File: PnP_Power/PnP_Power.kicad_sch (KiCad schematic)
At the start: 0 parts

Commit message: Progress
Schematic has everything but 12V jack and H-bridge Vac DC motor control
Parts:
- added A1: A000067, PnP_Footprints:ARDUINO_A000067, symbol PnP_symbols:A000067
- added C1, C2, C3, C4, C5, C6: 82uF, Capacitor_THT:CP_Radial_D8.0mm_P2.50mm, symbol Device:C_Polarized
- added D1, D2: GREEN, LED_SMD:LED_0603_1608Metric_Pad1.05x0.95mm_HandSolder, symbol Device:LED
- added J1: S2B-PH-K-SLFSN, PnP_Footprints:CONN_S2B-PH-K-S_JST, symbol PnP_symbols:S2B-PH-K-SLFSN
- added J2, J3, J4, J5, J6, J7: S4B-PH-K-SLFSN, PnP_Footprints:CONN_S4B-PH-K-S_JST, symbol PnP_symbols:S4B-PH-K-SLFSN
- added R1: 1.5k, Resistor_SMD:R_0603_1608Metric_Pad0.98x0.95mm_HandSolder, symbol Device:R_US
- added R2: 2.2k, Resistor_SMD:R_0603_1608Metric_Pad0.98x0.95mm_HandSolder, symbol Device:R_US
- added R3: 820, Resistor_SMD:R_0603_1608Metric_Pad0.98x0.95mm_HandSolder, symbol Device:R_US
- added U1, U2, U3, U4, U5, U6: ~, PnP_Footprints:A4988, symbol PnP_symbols:A4988
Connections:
- new net: J4.1, U3.6 (2B)
- new net: J4.2, U3.5 (2A)
- new net: J4.3, U3.4 (1A)
- new net: J4.4, U3.3 (1B)
- new net: D1.2 (A), R2.2
- new net: J5.1, U4.6 (2B)
- new net: J5.2, U4.5 (2A)
- new net: J5.3, U4.4 (1A)
- new net: J5.4, U4.3 (1B)
- new net: J7.1, U6.6 (2B)
- new net: J7.2, U6.5 (2A)
- new net: J7.3, U6.4 (1A)
- new net: J7.4, U6.3 (1B)
- new net: D2.2 (A), R3.2
- new net: J6.1, U5.6 (2B)
- new net: J6.2, U5.5 (2A)
- new net: J6.3, U5.4 (1A)
- new net: J6.4, U5.3 (1B)
- new net: J1.1, R1.2
- new net: J2.1, U1.6 (2B)
- new net: J2.2, U1.5 (2A)
- new net: J2.3, U1.4 (1A)
- new net: J2.4, U1.3 (1B)
- new net: J3.4, U2.3 (1B)
- new net: J3.3, U2.4 (1A)
- new net: J3.2, U2.5 (2A)
- new net: J3.1, U2.6 (2B)
- new net +12V: A1.VIN, C1.1, C2.1, C3.1, C4.1, C5.1, C6.1, R2.1, U1.8 (VMOT), U2.8 (VMOT), U3.8 (VMOT), U4.8 (VMOT), U5.8 (VMOT), U6.8 (VMOT)
- new net +5V: R3.1, U1.2 (VDD), U2.2 (VDD), U3.2 (VDD), U4.2 (VDD), U5.2 (VDD), U6.2 (VDD)
- new net DIR1: U1.9 (Direction)
- new net DIR2: U2.9 (Direction)
- new net DIR3: U3.9 (Direction)
- new net DIR4: U4.9 (Direction)
- new net DIR5: U5.9 (Direction)
- new net DIR6: U6.9 (Direction)
- new net EN1: U1.16 (ENABLE)
- new net EN2: U2.16 (ENABLE)
- new net EN3: U3.16 (ENABLE)
- new net EN4: U4.16 (ENABLE)
- new net EN5: U5.16 (ENABLE)
- new net EN6: U6.16 (ENABLE)
- new net GND: C1.2, C2.2, C3.2, C4.2, C5.2, C6.2, D1.1 (K), D2.1 (K), J1.2, U1.1 (GND), U1.7 (GND), U2.1 (GND), U2.7 (GND), U3.1 (GND), U3.7 (GND), U4.1 (GND), U4.7 (GND), U5.1 (GND), U5.7 (GND), U6.1 (GND), U6.7 (GND)
- new net MS1_1: U1.15 (MS1)
- new net MS1_2: U2.15 (MS1)
- new net MS1_3: U3.15 (MS1)
- new net MS1_4: U4.15 (MS1)
- new net MS1_5: U5.15 (MS1)
- new net MS1_6: U6.15 (MS1)
- new net MS2_1: U1.14 (MS2)
- new net MS2_2: U2.14 (MS2)
- new net MS2_3: U3.14 (MS2)
- new net MS2_4: U4.14 (MS2)
- new net MS2_5: U5.14 (MS2)
- new net MS2_6: U6.14 (MS2)
- new net MS3_1: U1.13 (MS3)
- new net MS3_2: U2.13 (MS3)
- new net MS3_3: U3.13 (MS3)
- new net MS3_4: U4.13 (MS3)
- new net MS3_5: U5.13 (MS3)
- new net MS3_6: U6.13 (MS3)
- new net RES1: U1.12 (Reset)
- new net RES2: U2.12 (Reset)
- new net RES3: U3.12 (Reset)
- new net RES4: U4.12 (Reset)
- new net RES5: U5.12 (Reset)
- new net RES6: U6.12 (Reset)
- new net SLP1: U1.11 (Sleep)
- new net SLP2: U2.11 (Sleep)
- new net SLP3: U3.11 (Sleep)
- new net SLP4: U4.11 (Sleep)
- new net SLP5: U5.11 (Sleep)
- new net SLP6: U6.11 (Sleep)
- new net STEP1: U1.10 (Step)
- new net STEP2: U2.10 (Step)
- new net STEP3: U3.10 (Step)
- new net STEP4: U4.10 (Step)
- new net STEP5: U5.10 (Step)
- new net STEP6: U6.10 (Step)
- new net WHITE_LED: R1.1
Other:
- note added: "NEMA 17 A Axis"
- note added: "NEMA 17 COMP FEED"
- note added: "NEMA 17 X Axis"
- note added: "NEMA 17 Y Axis 1"
- note added: "NEMA 17 Y Axis 2"
- note added: "NEMA 17 Z Axis"
- note added: "Power LEDs"
- note added: "White LED"

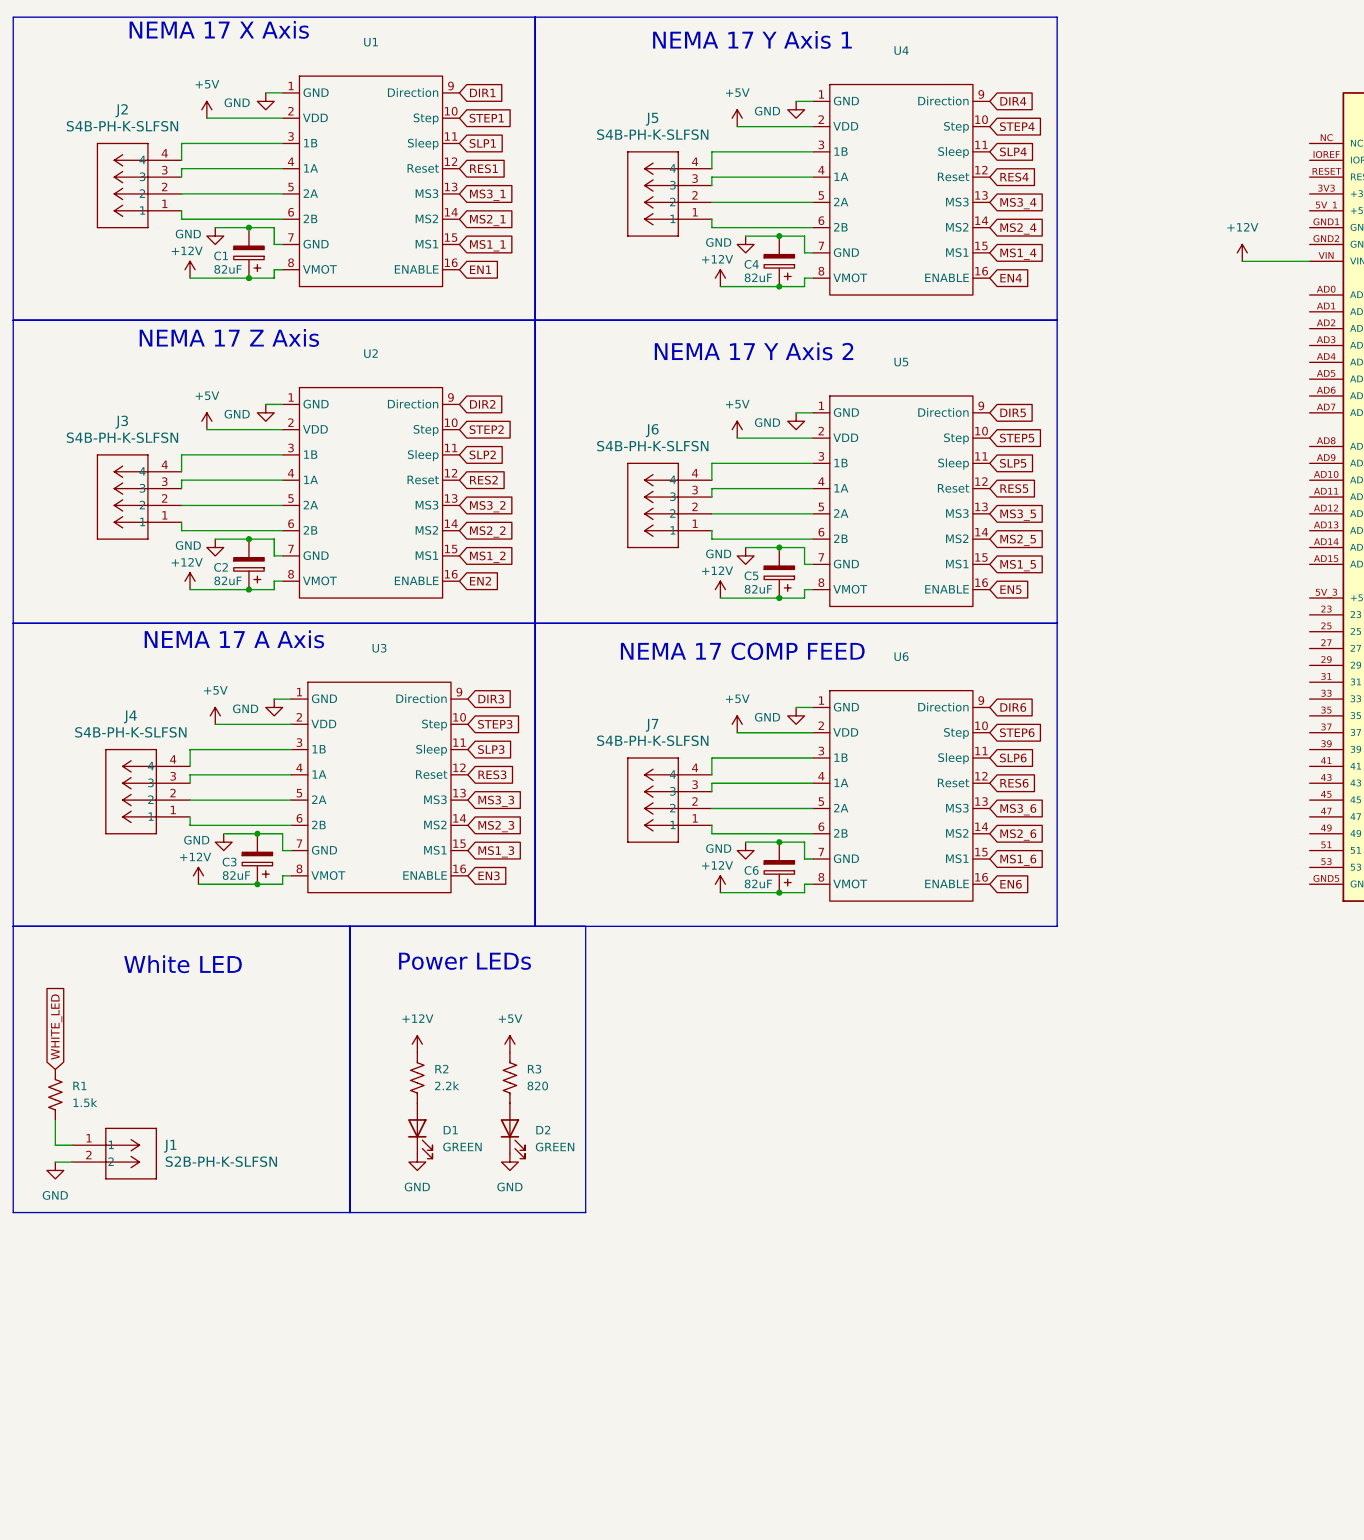
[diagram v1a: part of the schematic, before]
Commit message: Connectors changed, H-bridge VNH added, white leds done
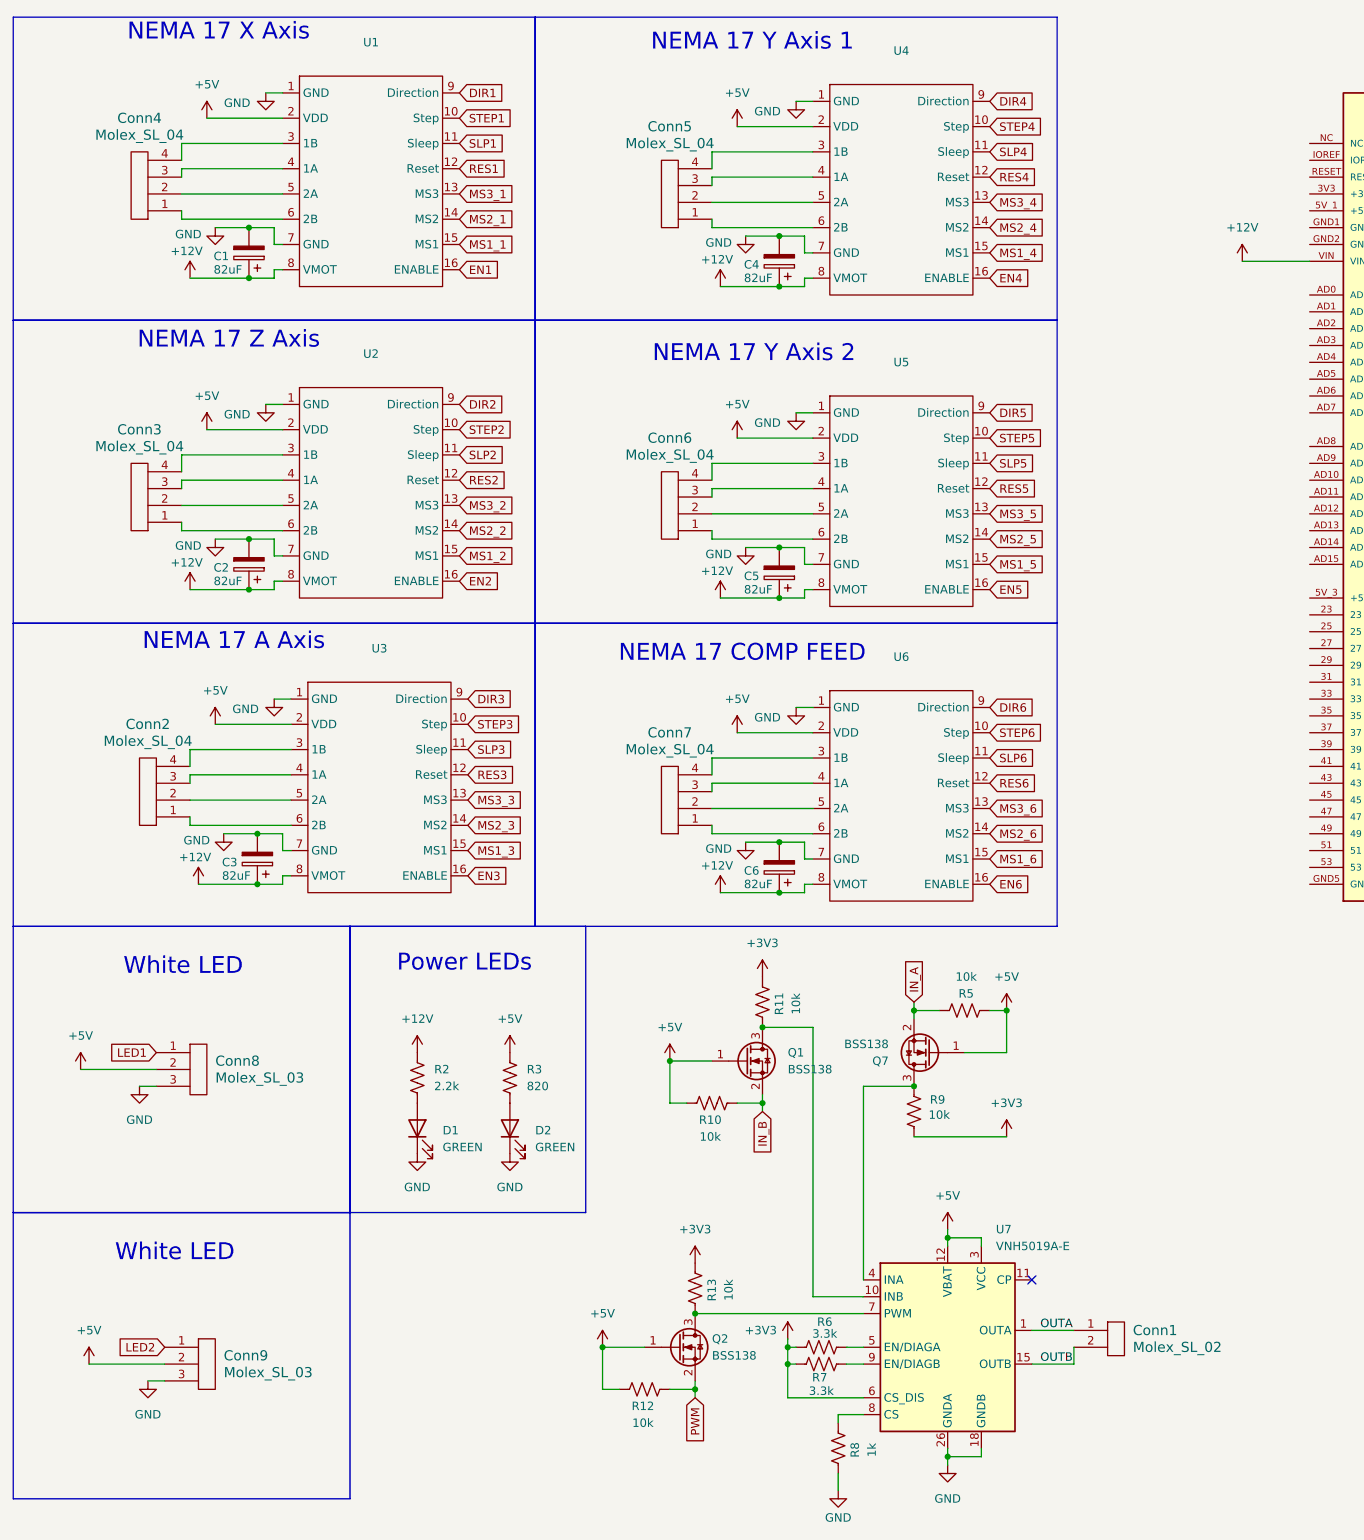
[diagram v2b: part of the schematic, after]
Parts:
- removed J1: S2B-PH-K-SLFSN, PnP_Footprints:CONN_S2B-PH-K-S_JST, symbol PnP_symbols:S2B-PH-K-SLFSN
- removed J2, J3, J4, J5, J6, J7: S4B-PH-K-SLFSN, PnP_Footprints:CONN_S4B-PH-K-S_JST, symbol PnP_symbols:S4B-PH-K-SLFSN
- removed R1: 1.5k, Resistor_SMD:R_0603_1608Metric_Pad0.98x0.95mm_HandSolder, symbol Device:R_US
- added Conn1: Molex_SL_02, symbol MRDT_Connectors:Molex_SL_02
- added Conn2, Conn3, Conn4, Conn5, Conn6, Conn7: Molex_SL_04, symbol MRDT_Connectors:Molex_SL_04
- added Conn8, Conn9: Molex_SL_03, symbol MRDT_Connectors:Molex_SL_03
- added Q1, Q2, Q7: BSS138, Package_TO_SOT_SMD:SOT-23, symbol Transistor_FET:BSS138
- added R10, R11, R12, R13, R5, R9: 10k, Resistor_SMD:R_0603_1608Metric_Pad0.98x0.95mm_HandSolder, symbol Device:R_US
- added R6, R7: 3.3k, Resistor_SMD:R_0603_1608Metric_Pad0.98x0.95mm_HandSolder, symbol Device:R_US
- added R8: 1k, Resistor_SMD:R_0603_1608Metric_Pad0.98x0.95mm_HandSolder, symbol Device:R_US
- added U7: VNH5019A-E, Package_SO:ST_MultiPowerSO-30, symbol Driver_Motor:VNH5019A-E
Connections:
- net +5V: now also Conn8.2, Conn9.2, Q1.1 (G), Q2.1 (G), Q7.1 (G), R10.2, R12.2, R5.2, U7.12 (VBAT), U7.13 (VCC), U7.23 (VCC), U7.3 (VCC), U7.31 (VCC)
- net GND: now also Conn8.3, Conn9.3, R8.2, U7.18 (GNDB), U7.19 (GNDB), U7.20 (GNDB), U7.26 (GNDA), U7.27 (GNDA), U7.28 (GNDA)
- net at U3.6 (2B): now also Conn2.1
- net at U3.5 (2A): now also Conn2.2
- net at U3.4 (1A): now also Conn2.3
- net at U3.3 (1B): now also Conn2.4
- net at U4.6 (2B): now also Conn5.1
- net at U4.5 (2A): now also Conn5.2
- net at U4.4 (1A): now also Conn5.3
- net at U4.3 (1B): now also Conn5.4
- net at U6.6 (2B): now also Conn7.1
- net at U6.5 (2A): now also Conn7.2
- net at U6.4 (1A): now also Conn7.3
- net at U6.3 (1B): now also Conn7.4
- net at U5.6 (2B): now also Conn6.1
- net at U5.5 (2A): now also Conn6.2
- net at U5.4 (1A): now also Conn6.3
- net at U5.3 (1B): now also Conn6.4
- net at U1.6 (2B): now also Conn4.1
- net at U1.5 (2A): now also Conn4.2
- net at U1.4 (1A): now also Conn4.3
- net at U1.3 (1B): now also Conn4.4
- net at U2.3 (1B): now also Conn3.4
- net at U2.4 (1A): now also Conn3.3
- net at U2.5 (2A): now also Conn3.2
- net at U2.6 (2B): now also Conn3.1
- new net: R7.2, U7.9 (EN/DIAGB)
- new net: R8.1, U7.8 (CS)
- new net: Q2.3 (D), R13.2, U7.7 (PWM)
- new net: Q7.3 (D), R9.2, U7.4 (INA)
- new net: Q1.3 (D), R11.2, U7.10 (INB)
- new net: R6.1, U7.5 (EN/DIAGA)
- new net +3V3: R11.1, R13.1, R6.2, R7.1, R9.1, U7.6 (CS_DIS)
- new net IN_A: Q7.2 (S), R5.1
- new net IN_B: Q1.2 (S), R10.1
- new net LED1: Conn8.1
- new net LED2: Conn9.1
- new net OUTA: Conn1.1, U7.1 (OUTA), U7.25 (OUTA), U7.30 (OUTA), U7.33 (OUTA)
- new net OUTB: Conn1.2, U7.15 (OUTB), U7.16 (OUTB), U7.21 (OUTB), U7.32 (OUTB)
- new net PWM: Q2.2 (S), R12.1
- no-connect marks 0 -> 1

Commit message: Schematic and Layout Changes
updated schematic logic
added limit switches
added 12V to 5V dc converter
added power jack
added jumpers
added inverter for DIRSW

Started layout placed and organized everything nice. Should need to be adjusted some and then routed.
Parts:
- removed Q1, Q2, Q7: BSS138, Package_TO_SOT_SMD:SOT-23, symbol Transistor_FET:BSS138
- removed R10, R11, R12, R13, R5, R9: 10k, Resistor_SMD:R_0603_1608Metric_Pad0.98x0.95mm_HandSolder, symbol Device:R_US
- added C7, C8: 22uF, Capacitor_SMD:C_0603_1608Metric_Pad1.08x0.95mm_HandSolder, symbol Device:C
- added C9: 0.1uF, Capacitor_SMD:C_0603_1608Metric_Pad1.08x0.95mm_HandSolder, symbol Device:C
- added Conn10, Conn11, Conn12, Conn13, Conn14, Conn15: Molex_SL_02, MRDT_Connectors:MOLEX_SL_02_Horizontal, symbol MRDT_Connectors:Molex_SL_02
- added J1: Barrel Jack 5mm x 2.5mm 54-00356, PnP_Footprints:TENSILITY_54-00356, symbol PnP_symbols:Barrel Jack 5mm x 2.5mm 54-00356
- added JP1, JP10, JP11, JP12, JP13, JP14, JP15, JP16, JP17, JP18, JP2, JP3, JP4, JP5, JP6, JP7, JP8, JP9: Jumper_2_Bridged, Connector_PinHeader_2.54mm:PinHeader_1x02_P2.54mm_Vertical, symbol Jumper:Jumper_2_Bridged
- added U8: LMS78_05-2.0R, PnP_Footprints:LMS78_05-2.0R, symbol PnP_symbols:LMS78_05-2.0R
- added U9: SN74LVC2G04DBVR, PnP_Footprints:SOT95P280X145-6N, symbol PnP_symbols:SN74LVC2G04DBVR
- C1, C2, C3, C4, C5, C6: footprint Capacitor_THT:CP_Radial_D8.0mm_P2.50mm -> Capacitor_THT:CP_Radial_D8.0mm_P3.50mm
- Conn1: footprint (none) -> MRDT_Connectors:MOLEX_SL_02_Horizontal
- Conn2, Conn3, Conn4, Conn5, Conn6, Conn7: footprint (none) -> MRDT_Connectors:MOLEX_SL_04_Horizontal
- Conn8, Conn9: footprint (none) -> MRDT_Connectors:MOLEX_SL_03_Horizontal
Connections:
- net RES1 is gone; now on net +5V: U1.12 (Reset)
- net RES2 is gone; now on net +5V: U2.12 (Reset)
- net RES3 is gone; now on net +5V: U3.12 (Reset)
- net RES4 is gone; now on net +5V: U4.12 (Reset)
- net RES5 is gone; now on net +5V: U5.12 (Reset)
- net RES6 is gone; now on net +5V: U6.12 (Reset)
- net SLP1 is gone; now on net +5V: U1.11 (Sleep)
- net SLP2 is gone; now on net +5V: U2.11 (Sleep)
- net SLP3 is gone; now on net +5V: U3.11 (Sleep)
- net SLP4 is gone; now on net +5V: U4.11 (Sleep)
- net SLP5 is gone; now on net +5V: U5.11 (Sleep)
- net SLP6 is gone; now on net +5V: U6.11 (Sleep)
- net +12V: now also C7.1, J1.A, U8.1 (Vi)
- net +3V3: now also A1.3V3 (+3V3)
- net +5V: now also A1.5V_1 (+5V_1), A1.5V_2 (+5V_2), A1.5V_3 (+5V_3), C8.1, C9.1, JP1.2 (B), JP10.2 (B), JP11.2 (B), JP12.2 (B), JP13.2 (B), JP14.2 (B), JP15.2 (B), JP16.2 (B), JP17.2 (B), JP18.2 (B), JP2.2 (B), JP3.2 (B), JP4.2 (B), JP5.2 (B), JP6.2 (B), JP7.2 (B), JP8.2 (B), JP9.2 (B), U8.3 (Vo), U9.5 (VCC)
- net DIR1: now also A1.51
- net DIR2: now also A1.34
- net DIR3: now also A1.28
- net DIR4: now also A1.48
- net DIR5: now also A1.AD7
- net DIR6: now also A1.AD1
- net EN1: now also A1.53
- net EN2: now also A1.30
- net EN3: now also A1.24
- net EN4: now also A1.AD8
- net EN5: now also A1.AD2
- net EN6: now also A1.38
- net GND: now also A1.GND1, A1.GND2, A1.GND3, A1.GND4, A1.GND5, C7.2, C8.2, C9.2, Conn10.2, Conn11.2, Conn12.2, Conn13.2, Conn14.2, Conn15.2, J1.B, U8.2 (GND), U9.2 (GND), U9.3 (2A)
- net LED1: now also A1.37
- net LED2: now also A1.39
- net PWM: now also A1.8, U7.7 (PWM)
- net STEP1: now also A1.49
- net STEP2: now also A1.36
- net STEP3: now also A1.26
- net STEP4: now also A1.46
- net STEP5: now also A1.AD6
- net STEP6: now also A1.AD0
- net VACDIR: now reaches U7.4 (INA)
- net VACDIR: now also A1.5, U9.1 (1A)
- net at U7.10 (INB): now also U9.6 (1Y)
- net LS1: now reaches A1.23
- net LS1: now also Conn10.1
- net LS2: now reaches A1.25
- net LS2: now also Conn11.1
- net LS3: now reaches A1.27
- net LS3: now also Conn12.1
- net LS4: now reaches A1.29
- net LS4: now also Conn13.1
- net LS5: now reaches A1.31
- net LS5: now also Conn14.1
- net LS6: now reaches A1.33
- net LS6: now also Conn15.1
- net MS1_1: no longer names the net of U1.15 (MS1)
- net MS1_1: now also JP9.1 (A)
- net MS1_2: no longer names the net of U2.15 (MS1)
- net MS1_2: now also JP6.1 (A)
- net MS1_3: no longer names the net of U3.15 (MS1)
- net MS1_3: now also JP3.1 (A)
- net MS1_4: no longer names the net of U4.15 (MS1)
- net MS1_4: now also JP18.1 (A)
- net MS1_5: no longer names the net of U5.15 (MS1)
- net MS1_5: now also JP15.1 (A)
- net MS1_6: no longer names the net of U6.15 (MS1)
- net MS1_6: now also JP12.1 (A)
- net MS2_1: no longer names the net of U1.14 (MS2)
- net MS2_1: now also JP8.1 (A)
- net MS2_2: no longer names the net of U2.14 (MS2)
- net MS2_2: now also JP5.1 (A)
- net MS2_3: no longer names the net of U3.14 (MS2)
- net MS2_3: now also JP2.1 (A)
- net MS2_4: no longer names the net of U4.14 (MS2)
- net MS2_4: now also JP17.1 (A)
- net MS2_5: no longer names the net of U5.14 (MS2)
- net MS2_5: now also JP14.1 (A)
- net MS2_6: no longer names the net of U6.14 (MS2)
- net MS2_6: now also JP11.1 (A)
- net MS3_1: no longer names the net of U1.13 (MS3)
- net MS3_1: now also JP7.1 (A)
- net MS3_2: no longer names the net of U2.13 (MS3)
- net MS3_2: now also JP4.1 (A)
- net MS3_3: no longer names the net of U3.13 (MS3)
- net MS3_3: now also JP1.1 (A)
- net MS3_4: no longer names the net of U4.13 (MS3)
- net MS3_4: now also JP16.1 (A)
- net MS3_5: no longer names the net of U5.13 (MS3)
- net MS3_5: now also JP13.1 (A)
- net MS3_6: no longer names the net of U6.13 (MS3)
- net MS3_6: now also JP10.1 (A)
- no-connect marks 1 -> 7
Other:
- note added: "12V Power In"
- note added: "5V DC Converter"
- note added: "Arduino Mega 2560"
- note added: "Full Bridge Motor Driver"
- note added: "Limit Switches"
- note added: "Logic Inverter"
- note added: "Vaccumm Motor Circuit"
- moved on the sheet: A1, C4, C5, C6, Conn1, Conn5, Conn6, Conn7, Conn8, Conn9, D1, D2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

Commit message: Idek
layouts and stuff and 3d model
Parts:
- added H1, H2, H3, H4: MountingHole, MountingHole:MountingHole_2.2mm_M2, symbol Mechanical:MountingHole
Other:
- note added: "Mounting Holes"
- moved on the sheet: A1
